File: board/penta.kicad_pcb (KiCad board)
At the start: 4 copper layers, 37.4 x 37.4 mm, 186 parts, among them J1 USB_C_Receptacle, J2 USB_C_Receptacle, J3 Conn_01x03_Pin, Q1 Q_NMOS_GSD, SW1 SW_Push, U1 3.3V LDO, U2 RP2040, U3 QSPI Flash, U4 MSUSB30, U5 USBLC6-2P6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

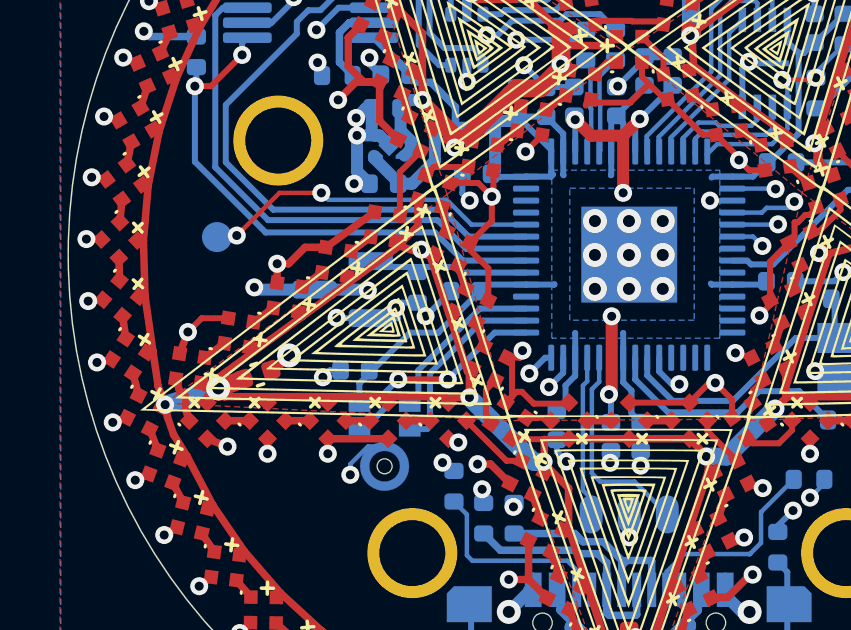
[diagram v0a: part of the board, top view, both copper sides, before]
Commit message: i did the freaking mosfet wrong *again*
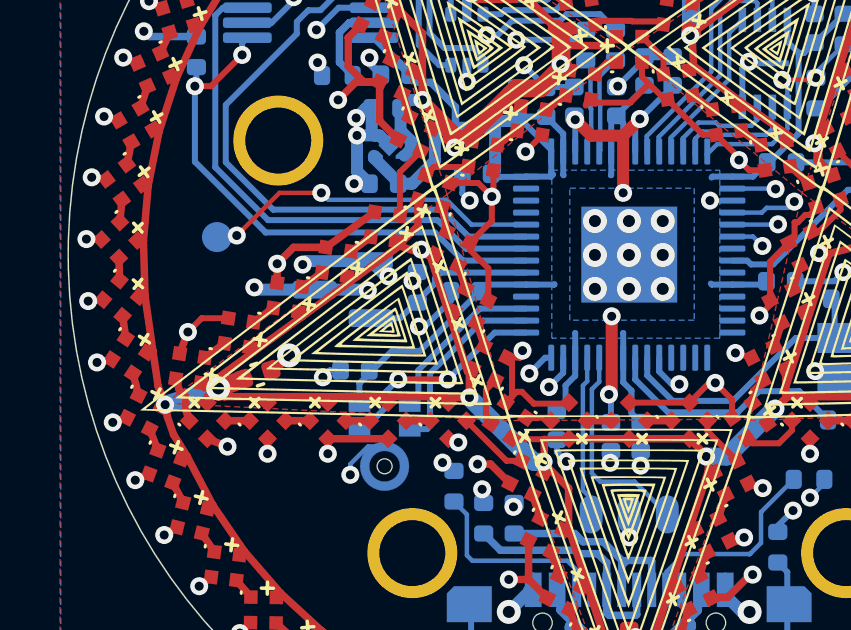
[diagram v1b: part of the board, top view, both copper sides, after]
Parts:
- Q1: value Q_NMOS_GSD -> Q_NMOS_SGD
- turned R12 to 90 degrees
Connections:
- Q1 pad 1: /EN_PIXELS -> GND
- Q1 pad 2: GND -> /EN_PIXELS
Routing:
- net GND: track 52.6 -> 53.5 mm, vias 51 -> 52

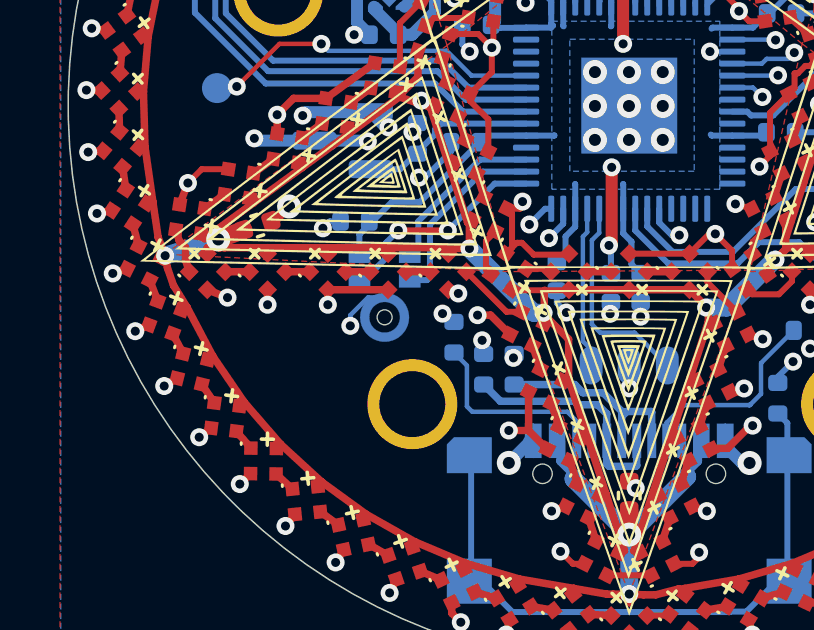
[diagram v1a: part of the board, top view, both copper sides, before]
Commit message: fix microphone GND connection (it didn't have one?! but is still working fine?!)
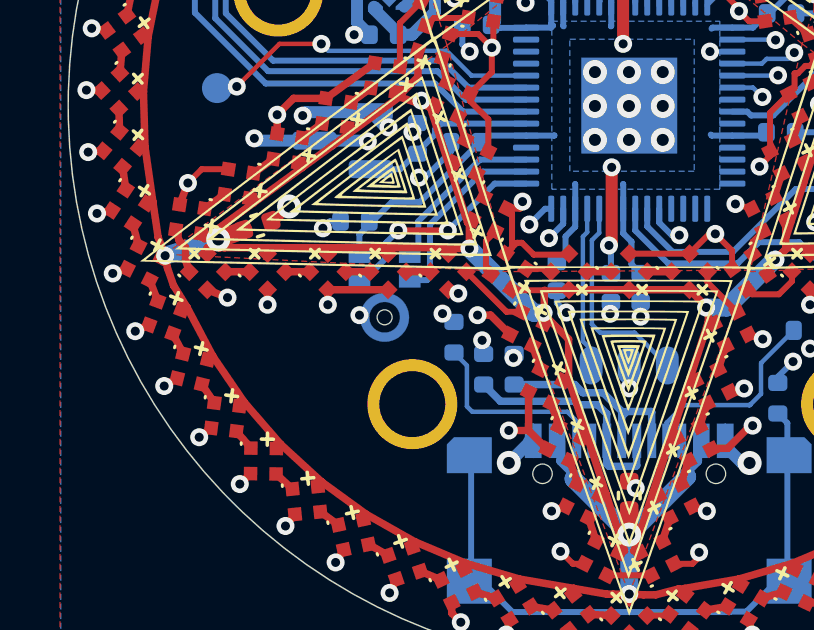
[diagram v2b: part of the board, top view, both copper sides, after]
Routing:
- net (no net): track 1.74 -> 0.00 mm, vias 1 -> 0
- net GND: track 53.5 -> 54.6 mm, vias 52 -> 53
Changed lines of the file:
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@@
 			(at 0.925 2.75 0)
 			(layer "B.SilkS")
-			(hide yes)
 			(effects
 				(font
@@
 			(pintype "unspecified")
 		)
-		(pad "3_1" smd custom
-			(at 0 -0.0475 180)
+		(pad "3" smd custom
+			(at 0 -1.3725 180)
 			(size 0.25 0.25)
 			(layers "B.Cu")
+			(net 2 "GND")
+			(pinfunction "GND")
+			(pintype "unspecified")
 			(options
 				(clearance outline)
@@
 				(gr_poly
 					(pts
-						(xy -0.5125 -0.6625) (xy -0.813 -0.6625) (xy -0.808 -0.5775) (xy -0.795 -0.4935) (xy -0.773 -0.4115)
-						(xy -0.742 -0.3325) (xy -0.704 -0.2565) (xy -0.657 -0.1845) (xy -0.604 -0.1185) (xy -0.544 -0.0585)
-						(xy -0.478 -0.0055) (xy -0.406 0.0415) (xy -0.33 0.0795) (xy -0.251 0.1105) (xy -0.169 0.1325)
-						(xy -0.085 0.1455) (xy 0 0.1505) (xy 0.085 0.1455) (xy 0.169 0.1325) (xy 0.251 0.1105) (xy 0.33 0.0795)
-						(xy 0.406 0.0415) (xy 0.478 -0.0055) (xy 0.544 -0.0585) (xy 0.604 -0.1185) (xy 0.657 -0.1845)
-						(xy 0.704 -0.2565) (xy 0.742 -0.3325) (xy 0.773 -0.4115) (xy 0.795 -0.4935) (xy 0.808 -0.5775)
-						(xy 0.813 -0.6625) (xy 0.512 -0.6625) (xy 0.51 -0.6085) (xy 0.501 -0.5555) (xy 0.487 -0.5045)
-						(xy 0.468 -0.4545) (xy 0.444 -0.4065) (xy 0.415 -0.3615) (xy 0.381 -0.3195) (xy 0.343 -0.2815)
-						(xy 0.301 -0.2475) (xy 0.256 -0.2185) (xy 0.208 -0.1945) (xy 0.158 -0.1755) (xy 0.107 -0.1615)
-						(xy 0.054 -0.1525) (xy 0 -0.1505) (xy -0.054 -0.1525) (xy -0.107 -0.1615) (xy -0.158 -0.1755)
-						(xy -0.208 -0.1945) (xy -0.256 -0.2185) (xy -0.301 -0.2475) (xy -0.343 -0.2815) (xy -0.381 -0.3195)
-						(xy -0.415 -0.3615) (xy -0.444 -0.4065) (xy -0.468 -0.4545) (xy -0.487 -0.5045) (xy -0.501 -0.5555)
-						(xy -0.51 -0.6085) (xy -0.512 -0.6625) (xy -0.5125 -0.6625)
+						(xy 0.5125 0.6625) (xy 0.813 0.6625) (xy 0.808 0.5775) (xy 0.795 0.4935) (xy 0.773 0.4115) (xy 0.742 0.3325)
+						(xy 0.704 0.2565) (xy 0.657 0.1845) (xy 0.604 0.1185) (xy 0.544 0.0585) (xy 0.478 0.0055) (xy 0.406 -0.0415)
+						(xy 0.33 -0.0795) (xy 0.251 -0.1105) (xy 0.169 -0.1325) (xy 0.085 -0.1455) (xy 0 -0.1495) (xy -0.085 -0.1455)
+						(xy -0.169 -0.1325) (xy -0.251 -0.1105) (xy -0.33 -0.0795) (xy -0.406 -0.0415) (xy -0.478 0.0055)
+						(xy -0.544 0.0585) (xy -0.604 0.1185) (xy -0.657 0.1845) (xy -0.704 0.2565) (xy -0.742 0.3325)
+						(xy -0.773 0.4115) (xy -0.795 0.4935) (xy -0.808 0.5775) (xy -0.813 0.6625) (xy -0.512 0.6625)
+						(xy -0.51 0.6085) (xy -0.501 0.5555) (xy -0.487 0.5045) (xy -0.468 0.4545) (xy -0.444 0.4065)
+						(xy -0.415 0.3615) (xy -0.381 0.3195) (xy -0.343 0.2815) (xy -0.301 0.2475) (xy -0.256 0.2185)
+						(xy -0.208 0.1945) (xy -0.158 0.1755) (xy -0.107 0.1615) (xy -0.054 0.1525) (xy 0 0.1505) (xy 0.054 0.1525)
+						(xy 0.107 0.1615) (xy 0.158 0.1755) (xy 0.208 0.1945) (xy 0.256 0.2185) (xy 0.301 0.2475) (xy 0.343 0.2815)
+						(xy 0.381 0.3195) (xy 0.415 0.3615) (xy 0.444 0.4065) (xy 0.468 0.4545) (xy 0.487 0.5045) (xy 0.501 0.5555)
+						(xy 0.51 0.6085) (xy 0.512 0.6625) (xy 0.5125 0.6625)
 					)
 					(width 0.01)
@@
 			)
 		)
-		(pad "3_2" smd custom
-			(at 0 -1.3725 180)
+		(pad "3" smd custom
+			(at 0 -0.0475 180)
 			(size 0.25 0.25)
 			(layers "B.Cu")
+			(net 2 "GND")
+			(pinfunction "GND")
+			(pintype "unspecified")
 			(options
 				(clearance outline)
@@
 				(gr_poly
 					(pts
-						(xy 0.5125 0.6625) (xy 0.813 0.6625) (xy 0.808 0.5775) (xy 0.795 0.4935) (xy 0.773 0.4115) (xy 0.742 0.3325)
-						(xy 0.704 0.2565) (xy 0.657 0.1845) (xy 0.604 0.1185) (xy 0.544 0.0585) (xy 0.478 0.0055) (xy 0.406 -0.0415)
-						(xy 0.33 -0.0795) (xy 0.251 -0.1105) (xy 0.169 -0.1325) (xy 0.085 -0.1455) (xy 0 -0.1495) (xy -0.085 -0.1455)
-						(xy -0.169 -0.1325) (xy -0.251 -0.1105) (xy -0.33 -0.0795) (xy -0.406 -0.0415) (xy -0.478 0.0055)
-						(xy -0.544 0.0585) (xy -0.604 0.1185) (xy -0.657 0.1845) (xy -0.704 0.2565) (xy -0.742 0.3325)
-						(xy -0.773 0.4115) (xy -0.795 0.4935) (xy -0.808 0.5775) (xy -0.813 0.6625) (xy -0.512 0.6625)
-						(xy -0.51 0.6085) (xy -0.501 0.5555) (xy -0.487 0.5045) (xy -0.468 0.4545) (xy -0.444 0.4065)
-						(xy -0.415 0.3615) (xy -0.381 0.3195) (xy -0.343 0.2815) (xy -0.301 0.2475) (xy -0.256 0.2185)
-						(xy -0.208 0.1945) (xy -0.158 0.1755) (xy -0.107 0.1615) (xy -0.054 0.1525) (xy 0 0.1505) (xy 0.054 0.1525)
-						(xy 0.107 0.1615) (xy 0.158 0.1755) (xy 0.208 0.1945) (xy 0.256 0.2185) (xy 0.301 0.2475) (xy 0.343 0.2815)
-						(xy 0.381 0.3195) (xy 0.415 0.3615) (xy 0.444 0.4065) (xy 0.468 0.4545) (xy 0.487 0.5045) (xy 0.501 0.5555)
-						(xy 0.51 0.6085) (xy 0.512 0.6625) (xy 0.5125 0.6625)
+						(xy -0.5125 -0.6625) (xy -0.813 -0.6625) (xy -0.808 -0.5775) (xy -0.795 -0.4935) (xy -0.773 -0.4115)
+						(xy -0.742 -0.3325) (xy -0.704 -0.2565) (xy -0.657 -0.1845) (xy -0.604 -0.1185) (xy -0.544 -0.0585)
+						(xy -0.478 -0.0055) (xy -0.406 0.0415) (xy -0.33 0.0795) (xy -0.251 0.1105) (xy -0.169 0.1325)
+						(xy -0.085 0.1455) (xy 0 0.1505) (xy 0.085 0.1455) (xy 0.169 0.1325) (xy 0.251 0.1105) (xy 0.33 0.0795)
+						(xy 0.406 0.0415) (xy 0.478 -0.0055) (xy 0.544 -0.0585) (xy 0.604 -0.1185) (xy 0.657 -0.1845)
+						(xy 0.704 -0.2565) (xy 0.742 -0.3325) (xy 0.773 -0.4115) (xy 0.795 -0.4935) (xy 0.808 -0.5775)
+						(xy 0.813 -0.6625) (xy 0.512 -0.6625) (xy 0.51 -0.6085) (xy 0.501 -0.5555) (xy 0.487 -0.5045)
+						(xy 0.468 -0.4545) (xy 0.444 -0.4065) (xy 0.415 -0.3615) (xy 0.381 -0.3195) (xy 0.343 -0.2815)
+						(xy 0.301 -0.2475) (xy 0.256 -0.2185) (xy 0.208 -0.1945) (xy 0.158 -0.1755) (xy 0.107 -0.1615)
+						(xy 0.054 -0.1525) (xy 0 -0.1505) (xy -0.054 -0.1525) (xy -0.107 -0.1615) (xy -0.158 -0.1755)
+						(xy -0.208 -0.1945) (xy -0.256 -0.2185) (xy -0.301 -0.2475) (xy -0.343 -0.2815) (xy -0.381 -0.3195)
+						(xy -0.415 -0.3615) (xy -0.444 -0.4065) (xy -0.468 -0.4545) (xy -0.487 -0.5045) (xy -0.501 -0.5555)
+						(xy -0.51 -0.6085) (xy -0.512 -0.6625) (xy -0.5125 -0.6625)
 					)
 					(width 0.01)
@@
 		)
 	)
-	(via
-		(at 90.7034 107.3404)
-		(size 0.6)
-		(drill 0.3)
-		(layers "F.Cu" "B.Cu")
-		(net 0)
-	)
-	(segment
-		(start 90.7034 106.9848)
-		(end 90.7034 107.3404)
-		(width 0.15)
-		(layer "B.Cu")
-		(net 0)
-	)
-	(segment
-		(start 91.8464 106.393992)
-		(end 91.294208 106.393992)
-		(width 0.15)
-		(layer "B.Cu")
-		(net 0)
-	)
-	(segment
-		(start 91.294208 106.393992)
-		(end 90.7034 106.9848)
-		(width 0.15)
-		(layer "B.Cu")
-		(net 0)
-	)
 	(segment
 		(start 94.611183 103.898337)
@@
 	)
 	(via
+		(at 91.0082 106.9848)
+		(size 0.6)
+		(drill 0.3)
+		(layers "F.Cu" "B.Cu")
+		(net 2)
+	)
+	(via
 		(at 90.8304 97.6376)
 		(size 0.6)
@@
 	)
 	(segment
+		(start 91.0082 106.9848)
+		(end 91.599008 106.393992)
+		(width 0.15)
+		(layer "B.Cu")
+		(net 2)
+	)
+	(segment
 		(start 99.3902 106.5504)
 		(end 99.3902 106.9146)
@@
 		(layer "B.Cu")
 		(net 2)
+	)
+	(segment
+		(start 91.599008 106.393992)
+		(end 91.8464 106.393992)
+		(width 0.15)
+		(layer "B.Cu")
+		(net 2)
